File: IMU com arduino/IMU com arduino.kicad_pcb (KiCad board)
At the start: 2 copper layers, 2 parts, among them J1 IMU

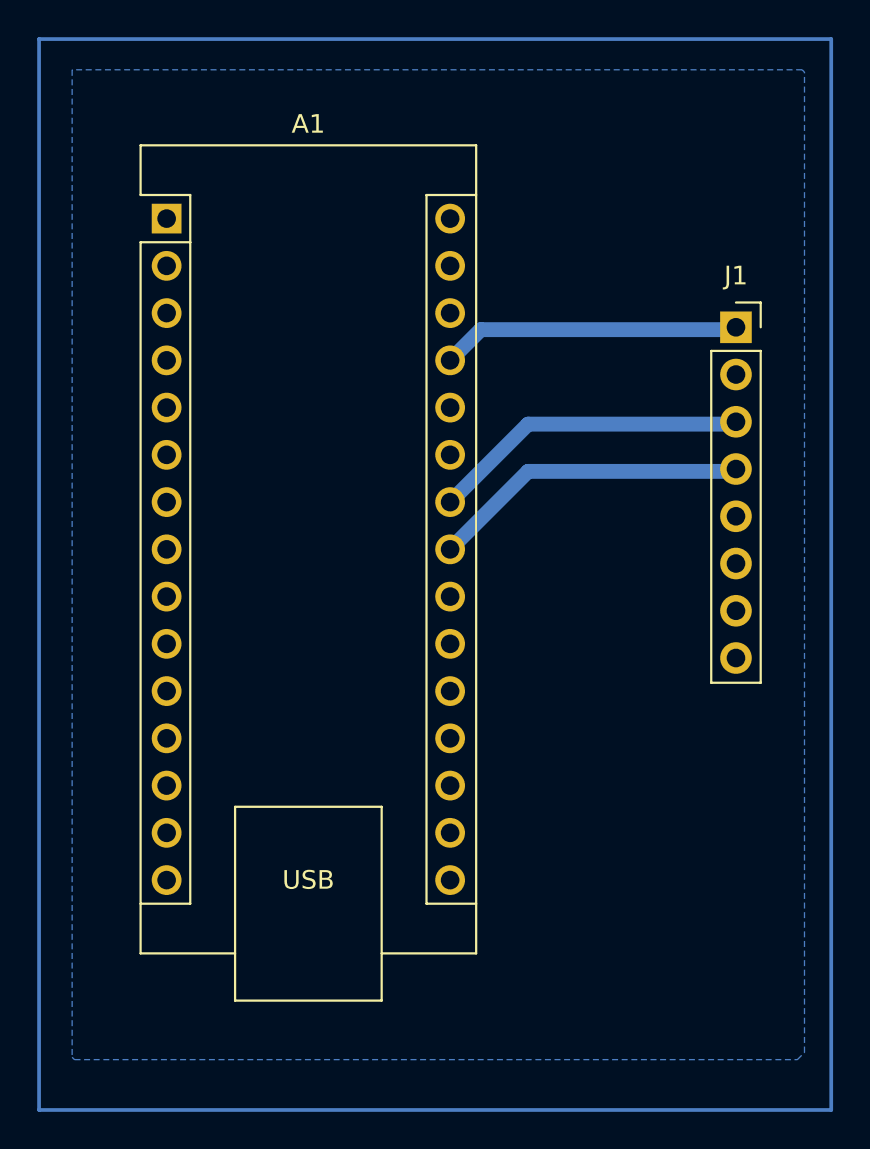
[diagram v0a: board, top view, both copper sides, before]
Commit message: Adionei o arduino na placa integrada (nao terminei) Adicionei a pasta de teclado (projeto pessoal)
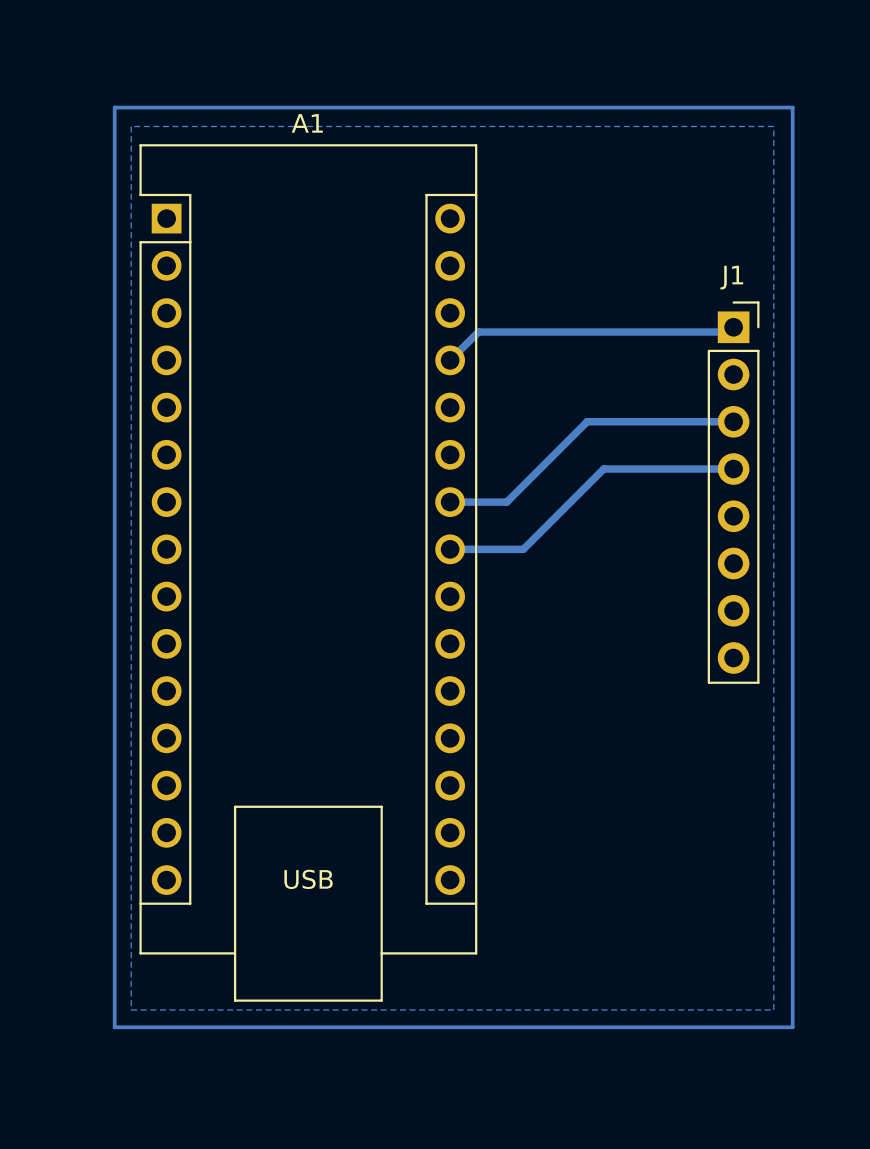
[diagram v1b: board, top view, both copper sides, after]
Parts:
- moved J1 0.13 mm to (162.7, 80.0)
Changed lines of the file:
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@@
 	(footprint "Connector_PinSocket_2.54mm:PinSocket_1x08_P2.54mm_Vertical"
 		(layer "F.Cu")
-		(at 162.814 80.01)
+		(at 162.687 80.01)
 		(descr "Through hole straight socket strip, 1x08, 2.54mm pitch, single row (from Kicad 4.0.7), script generated")
 		(tags "Through hole socket strip THT 1x08 2.54mm single row")
@@
 	)
 	(gr_rect
-		(start 125.349 64.516)
-		(end 167.934 122.087)
+		(start 129.413 68.199)
+		(end 165.862 117.642)
 		(stroke
 			(width 0.2)
@@
 		(fill none)
 		(layer "B.Cu")
+		(net 33)
 	)
 	(segment
-		(start 149.098 80.137)
-		(end 162.814 80.137)
-		(width 0.8)
+		(start 147.447 81.788)
+		(end 148.971 80.264)
+		(width 0.4)
 		(layer "B.Cu")
 		(net 3)
 	)
 	(segment
-		(start 147.447 81.788)
-		(end 149.098 80.137)
-		(width 0.8)
+		(start 148.971 80.264)
+		(end 162.433 80.264)
+		(width 0.4)
 		(layer "B.Cu")
 		(net 3)
 	)
 	(segment
-		(start 151.638 85.217)
-		(end 162.814 85.217)
-		(width 0.8)
+		(start 162.433 80.264)
+		(end 162.687 80.01)
+		(width 0.2)
+		(layer "B.Cu")
+		(net 3)
+	)
+	(segment
+		(start 150.495 89.408)
+		(end 154.813 85.09)
+		(width 0.4)
 		(layer "B.Cu")
 		(net 7)
@@
 	(segment
 		(start 147.447 89.408)
-		(end 151.638 85.217)
-		(width 0.8)
+		(end 150.495 89.408)
+		(width 0.4)
+		(layer "B.Cu")
+		(net 7)
+	)
+	(segment
+		(start 154.813 85.09)
+		(end 162.687 85.09)
+		(width 0.4)
 		(layer "B.Cu")
 		(net 7)
@@
 	)
 	(segment
-		(start 151.638 87.757)
-		(end 162.814 87.757)
-		(width 0.8)
+		(start 151.384 91.948)
+		(end 155.702 87.63)
+		(width 0.4)
 		(layer "B.Cu")
 		(net 9)
@@
 	(segment
 		(start 147.447 91.948)
-		(end 151.638 87.757)
-		(width 0.8)
+		(end 151.384 91.948)
+		(width 0.4)
+		(layer "B.Cu")
+		(net 9)
+	)
+	(segment
+		(start 155.702 87.63)
+		(end 162.687 87.63)
+		(width 0.4)
 		(layer "B.Cu")
 		(net 9)
@@
 		(filled_areas_thickness no)
 		(fill yes
-			(thermal_gap 0.5)
-			(thermal_bridge_width 0.5)
+			(thermal_gap 0.4)
+			(thermal_bridge_width 0.8)
 		)
 		(polygon
 			(pts
-				(xy 127.127 119.253) (xy 127.254 119.38) (xy 166.116 119.38) (xy 166.497 118.999) (xy 166.497 66.294)
-				(xy 166.37 66.167) (xy 127.127 66.167)
-			)
-		)
+				(xy 130.302 69.215) (xy 130.302 116.713) (xy 164.846 116.713) (xy 164.846 69.215)
+			)
+		)
